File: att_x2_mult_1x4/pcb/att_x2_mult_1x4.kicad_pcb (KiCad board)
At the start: 2 copper layers, 17.8 x 95.2 mm, 13 parts, among them J1 AudioJack2_SwitchT, J2 AudioJack2_SwitchT, J3 AudioJack2_SwitchT, J4 AudioJack2_SwitchT, J5 AudioJack2_SwitchT, J6 AudioJack2_SwitchT, J7 AudioJack2_SwitchT, J8 AudioJack2_SwitchT

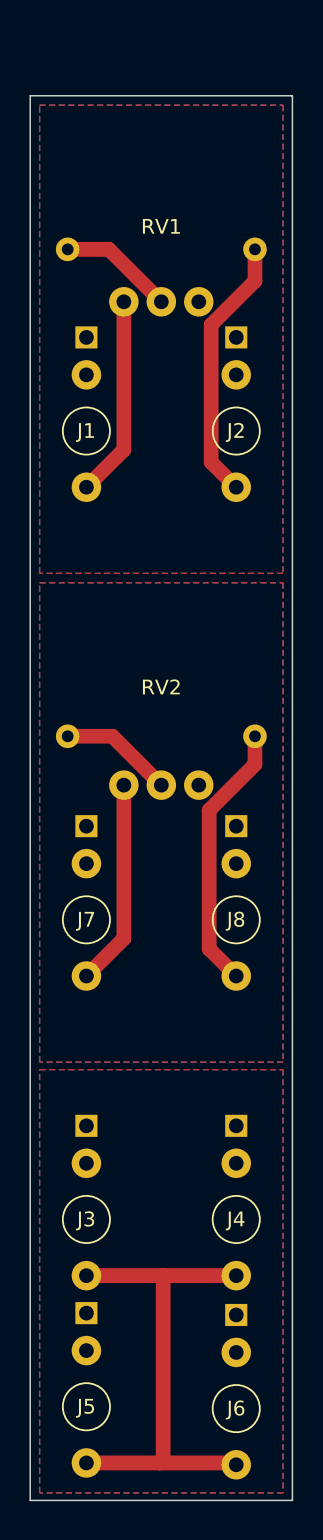
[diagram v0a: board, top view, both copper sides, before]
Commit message: moved resistor, added scale to panel
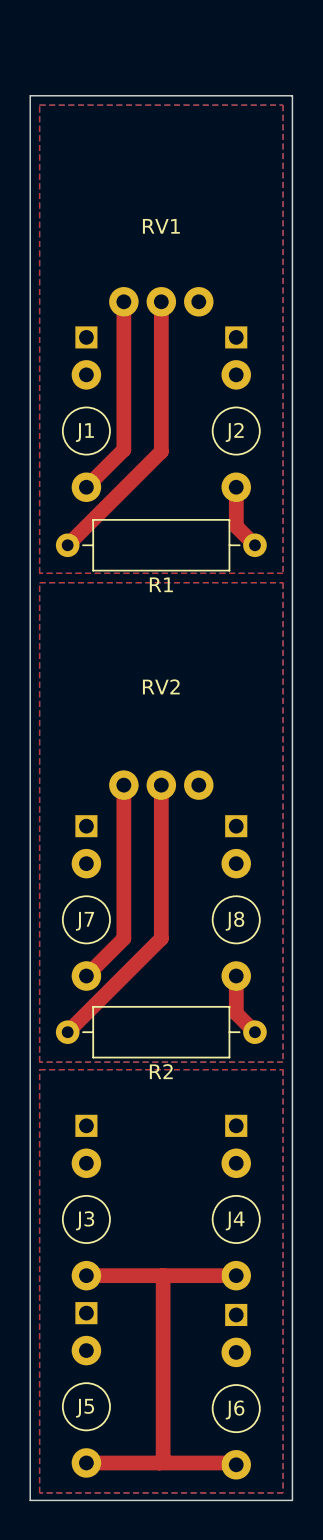
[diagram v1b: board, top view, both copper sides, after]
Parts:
- R1, R2: moved to F.Cu
- moved R1 20.1 mm to (108.0, 105.4)
- moved R2 20.1 mm to (108.0, 138.4)
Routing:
- net Net-(J8-PadT): track 18.3 -> 4.34 mm
- net Net-(J2-PadT): track 18.1 -> 4.46 mm
- net Net-(RV2-Pad2): track 7.72 -> 19.4 mm
- net Net-(RV1-Pad2): track 7.82 -> 19.1 mm
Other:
- board text added: "MB20220612"
- board text removed: "MB20220604"

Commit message: moved second attenuator slightly down
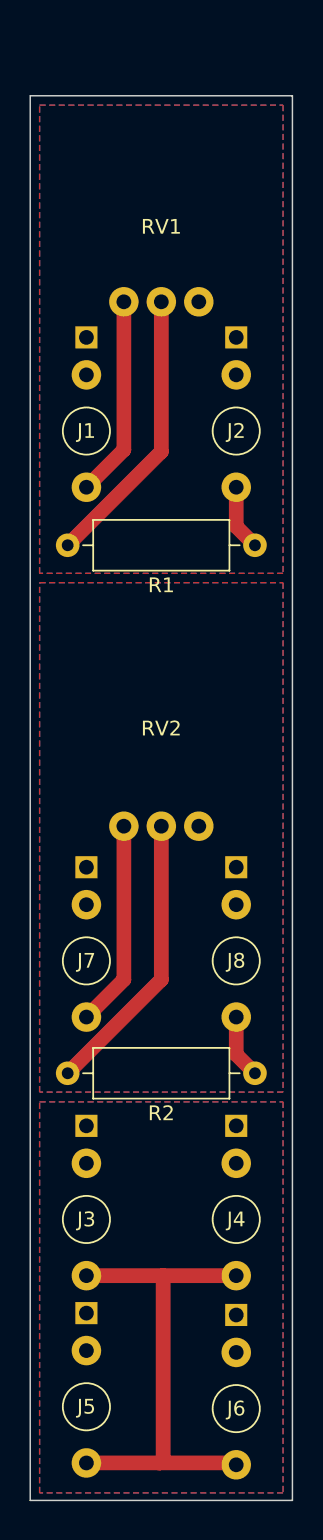
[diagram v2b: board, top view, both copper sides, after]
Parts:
- moved J7 2.78 mm to (96.5, 137.4)
- moved J8 2.78 mm to (106.7, 137.4)
- moved R2 2.78 mm to (108.0, 141.2)
- moved RV2 2.78 mm to (99.1, 124.5)
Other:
- board text added: "MB20220617"
- board text removed: "MB20220612"
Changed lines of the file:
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@@
   (net 15 "Net-(J8-PadT)")
   (net 16 "unconnected-(J8-PadTN)")
-  (net 17 "Net-(RV1-Pad2)")
-  (net 18 "Net-(RV2-Pad2)")
+  (net 17 "Net-(R1-Pad2)")
+  (net 18 "Net-(R2-Pad2)")
   (footprint "eurorack_footprints:audio_jack_pj-398sm" (layer "F.Cu")
     (at 106.68 167.765)
@@
   )
   (footprint "eurorack_footprints:audio_jack_pj-398sm" (layer "F.Cu")
-    (at 96.52 134.62)
+    (at 96.52 137.404)
     (property "Sheetfile" "att_x2_mult_1x4.kicad_sch")
     (property "Sheetname" "")
@@
       (net 2 "Net-(J1-PadT)") (pinfunction "1") (pintype "passive"))
     (pad "2" thru_hole circle (at 2.54 0) (size 2 2) (drill 1) (layers *.Cu *.Mask)
-      (net 17 "Net-(RV1-Pad2)") (pinfunction "2") (pintype "passive"))
+      (net 17 "Net-(R1-Pad2)") (pinfunction "2") (pintype "passive"))
     (pad "3" thru_hole circle (at 5.08 0) (size 2 2) (drill 1) (layers *.Cu *.Mask)
       (net 1 "/gnd1") (pinfunction "3") (pintype "passive"))
   )
   (footprint "Resistor_THT:R_Axial_DIN0309_L9.0mm_D3.2mm_P12.70mm_Horizontal" (layer "F.Cu")
-    (at 107.95 138.43 180)
+    (at 107.95 141.214 180)
     (descr "Resistor, Axial_DIN0309 series, Axial, Horizontal, pin pitch=12.7mm, 0.5W = 1/2W, length*diameter=9*3.2mm^2, http://cdn-reichelt.de/documents/datenblatt/B400/1_4W%23YAG.pdf")
     (tags "Resistor Axial_DIN0309 series Axial Horizontal pin pitch 12.7mm 0.5W = 1/2W length 9mm diameter 3.2mm")
@@
       (net 15 "Net-(J8-PadT)") (pintype "passive"))
     (pad "2" thru_hole oval (at 12.7 0 180) (size 1.6 1.6) (drill 0.8) (layers *.Cu *.Mask)
-      (net 18 "Net-(RV2-Pad2)") (pintype "passive"))
+      (net 18 "Net-(R2-Pad2)") (pintype "passive"))
     (model "${KICAD6_3DMODEL_DIR}/Resistor_THT.3dshapes/R_Axial_DIN0309_L9.0mm_D3.2mm_P12.70mm_Horizontal.wrl"
       (offset (xyz 0 0 0))
@@
   )
   (footprint "eurorack_footprints:pot1_A" (layer "F.Cu")
-    (at 99.06 121.6765)
+    (at 99.06 124.4605)
     (property "Sheetfile" "att_x2_mult_1x4.kicad_sch")
     (property "Sheetname" "")
@@
       (net 13 "Net-(J7-PadT)") (pinfunction "1") (pintype "passive"))
     (pad "2" thru_hole circle (at 2.54 0) (size 2 2) (drill 1) (layers *.Cu *.Mask)
-      (net 18 "Net-(RV2-Pad2)") (pinfunction "2") (pintype "passive"))
+      (net 18 "Net-(R2-Pad2)") (pinfunction "2") (pintype "passive"))
     (pad "3" thru_hole circle (at 5.08 0) (size 2 2) (drill 1) (layers *.Cu *.Mask)
       (net 12 "/gnd2") (pinfunction "3") (pintype "passive"))
@@
   )
   (footprint "eurorack_footprints:audio_jack_pj-398sm" (layer "F.Cu")
-    (at 106.68 134.62)
+    (at 106.68 137.404)
     (property "Sheetfile" "att_x2_mult_1x4.kicad_sch")
     (property "Sheetname" "")
@@
       (net 4 "Net-(J2-PadT)") (pintype "passive"))
     (pad "2" thru_hole oval (at 12.7 0 180) (size 1.6 1.6) (drill 0.8) (layers *.Cu *.Mask)
-      (net 17 "Net-(RV1-Pad2)") (pintype "passive"))
+      (net 17 "Net-(R1-Pad2)") (pintype "passive"))
     (model "${KICAD6_3DMODEL_DIR}/Resistor_THT.3dshapes/R_Axial_DIN0309_L9.0mm_D3.2mm_P12.70mm_Horizontal.wrl"
       (offset (xyz 0 0 0))
@@
     (effects (font (size 1.5 1.5) (thickness 0.3)) (justify mirror))
   )
-  (gr_text "MB20220612\n" (at 101.6 165.1) (layer "B.SilkS")
+  (gr_text "MB20220617\n" (at 101.6 165.1) (layer "B.SilkS")
     (effects (font (size 1 1) (thickness 0.15)) (justify mirror))
   )
@@
   (segment (start 101.475 167.64) (end 106.555 167.64) (width 1) (layer "F.Cu") (net 7))
   (segment (start 101.725 154.94) (end 101.725 167.39) (width 1) (layer "F.Cu") (net 7))
-  (segment (start 99.06 132.08) (end 99.06 122.045) (width 1) (layer "F.Cu") (net 13))
-  (segment (start 96.52 134.62) (end 99.06 132.08) (width 1) (layer "F.Cu") (net 13))
-  (segment (start 106.68 134.62) (end 106.68 137.16) (width 1) (layer "F.Cu") (net 15))
-  (segment (start 106.68 137.16) (end 107.95 138.43) (width 1) (layer "F.Cu") (net 15))
+  (segment (start 99.06 134.864) (end 99.06 124.829) (width 1) (layer "F.Cu") (net 13))
+  (segment (start 96.52 137.404) (end 99.06 134.864) (width 1) (layer "F.Cu") (net 13))
+  (segment (start 106.68 137.404) (end 106.68 139.944) (width 1) (layer "F.Cu") (net 15))
+  (segment (start 106.68 139.944) (end 107.95 141.214) (width 1) (layer "F.Cu") (net 15))
   (segment (start 95.25 105.41) (end 101.6 99.06) (width 1) (layer "F.Cu") (net 17))
   (segment (start 101.6 99.06) (end 101.6 88.9) (width 1) (layer "F.Cu") (net 17))
-  (segment (start 95.25 138.43) (end 101.6 132.08) (width 1) (layer "F.Cu") (net 18))
-  (segment (start 101.6 132.08) (end 101.6 121.6765) (width 1) (layer "F.Cu") (net 18))
+  (segment (start 95.25 141.214) (end 101.6 134.864) (width 1) (layer "F.Cu") (net 18))
+  (segment (start 101.6 134.864) (end 101.6 124.4605) (width 1) (layer "F.Cu") (net 18))
   (zone (net 6) (net_name "/gnd3") (layers F&B.Cu) (hatch edge 0.508)
     (connect_pads (clearance 0.508))
@@
         (xy 109.855 169.67)
         (xy 93.345 169.67)
-        (xy 93.345 140.97)
-        (xy 109.855 140.97)
+        (xy 93.345 143.1544)
+        (xy 109.855 143.1544)
       )
     )
@@
     (polygon
       (pts
-        (xy 109.855 140.46)
-        (xy 93.345 140.46)
+        (xy 109.855 142.492)
+        (xy 93.345 142.492)
         (xy 93.345 107.95)
         (xy 109.855 107.95)

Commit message: replaced tht resistor with an smd
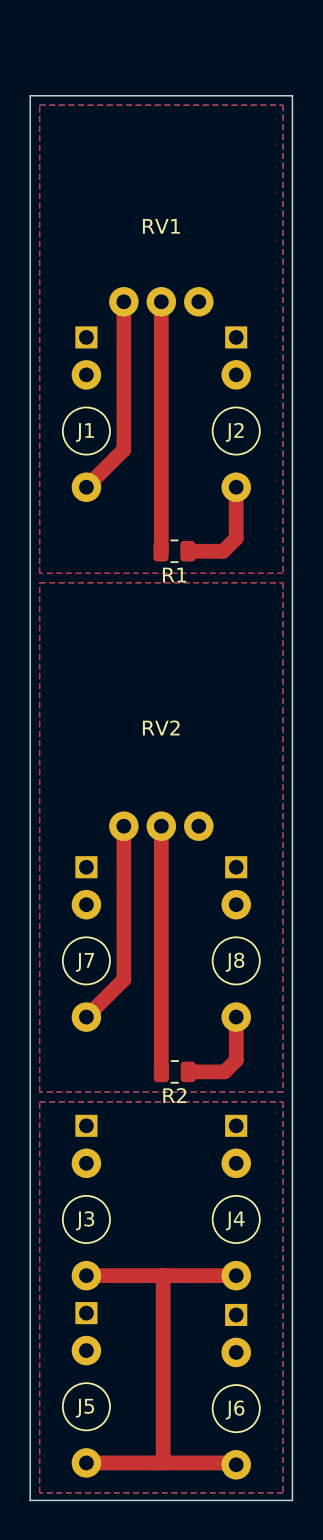
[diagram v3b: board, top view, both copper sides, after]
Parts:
- R1, R2: footprint Resistor_THT:R_Axial_DIN0309_L9.0mm_D3.2mm_P12.70mm_Horizontal -> Resistor_SMD:R_0805_2012Metric
- moved R1 5.48 mm to (102.5, 105.8)
- moved R2 5.44 mm to (102.5, 141.1)
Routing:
- net Net-(R2-Pad2): track 19.4 -> 16.2 mm
- net Net-(J2-PadT): track 4.46 -> 7.11 mm
- net Net-(R1-Pad2): track 19.1 -> 16.9 mm
- net Net-(J8-PadT): track 4.34 -> 6.51 mm

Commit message: updated pot footprint, changed rout back to tht
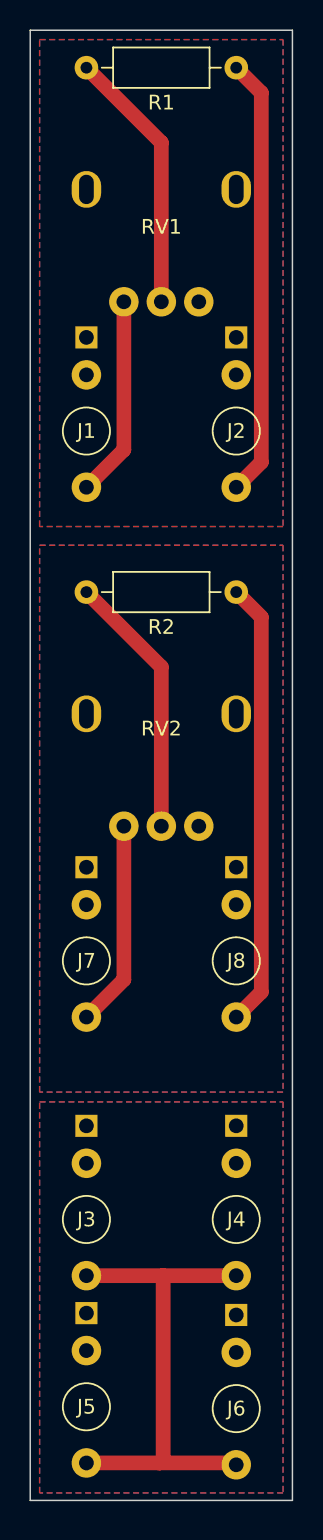
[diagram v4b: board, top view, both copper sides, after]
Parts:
- R1, R2: footprint Resistor_SMD:R_0805_2012Metric -> Resistor_THT:R_Axial_DIN0207_L6.3mm_D2.5mm_P10.16mm_Horizontal
- moved R1 33.1 mm to (106.7, 73.0)
- moved R2 32.8 mm to (106.7, 108.6)
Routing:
- net Net-(J8-PadT): track 6.51 -> 30.2 mm
- net Net-(J2-PadT): track 7.11 -> 29.9 mm
- net Net-(R2-Pad2): track 16.2 -> 18.0 mm
- net Net-(R1-Pad2): track 16.9 -> 18.0 mm
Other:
- board size 17.8 x 95.2 mm -> 17.8 x 99.7 mm
- board text added: "MB20220622"
- board text removed: "MB20220617"

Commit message: reverted panel ; change pot direction
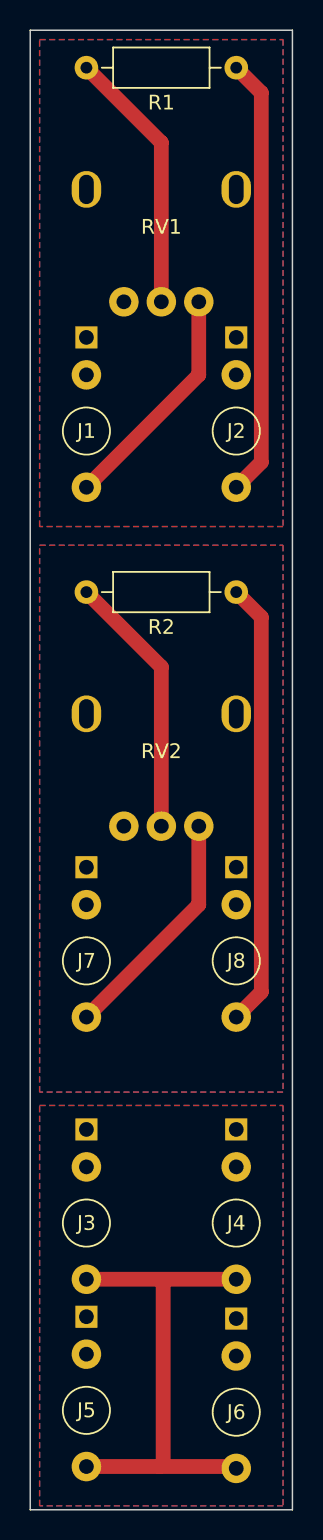
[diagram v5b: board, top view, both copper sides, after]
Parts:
- RV1, RV2: footprint eurorack_footprints:pot1_A -> eurorack_footprints:pot1_B
- moved G*** 0.24 mm to (101.6, 151.4)
- moved J3 0.24 mm to (96.5, 155.2)
- moved J4 0.24 mm to (106.7, 155.2)
- moved J5 0.24 mm to (96.5, 167.9)
- moved J6 0.24 mm to (106.7, 168.0)
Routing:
- net Net-(J7-PadT): track 13.6 -> 16.1 mm
- net Net-(J1-PadT): track 13.6 -> 15.7 mm
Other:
- board size 17.8 x 99.7 mm -> 17.8 x 100.3 mm
- board text added: "MB20220708"
- board text removed: "MB20220622"
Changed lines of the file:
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@@
   (net 18 "Net-(R2-Pad2)")
   (footprint "eurorack_footprints:audio_jack_pj-398sm" (layer "F.Cu")
-    (at 106.68 167.765)
+    (at 106.68 168.00884)
     (property "Sheetfile" "att_x2_mult_1x4.kicad_sch")
     (property "Sheetname" "")
@@
   )
   (footprint "eurorack_footprints:audio_jack_pj-398sm" (layer "F.Cu")
-    (at 96.52 154.94)
+    (at 96.52 155.18384)
     (property "Sheetfile" "att_x2_mult_1x4.kicad_sch")
     (property "Sheetname" "")
@@
       (net 8 "unconnected-(J3-PadTN)") (pintype "passive"))
   )
-  (footprint "eurorack_footprints:pot1_A" (layer "F.Cu")
+  (footprint "eurorack_footprints:pot1_B" (layer "F.Cu")
     (at 99.06 88.9)
     (property "Sheetfile" "att_x2_mult_1x4.kicad_sch")
@@
     (pad "" thru_hole oval (at 7.62 -7.62 90) (size 2.5 2) (drill oval 2 1) (layers *.Cu *.Mask))
     (pad "" thru_hole oval (at -2.54 -7.62 90) (size 2.5 2) (drill oval 2 1) (layers *.Cu *.Mask))
-    (pad "1" thru_hole circle (at 0 0) (size 2 2) (drill 1) (layers *.Cu *.Mask)
+    (pad "1" thru_hole circle (at 5.08 0) (size 2 2) (drill 1) (layers *.Cu *.Mask)
       (net 2 "Net-(J1-PadT)") (pinfunction "1") (pintype "passive"))
     (pad "2" thru_hole circle (at 2.54 0) (size 2 2) (drill 1) (layers *.Cu *.Mask)
       (net 17 "Net-(R1-Pad2)") (pinfunction "2") (pintype "passive"))
-    (pad "3" thru_hole circle (at 5.08 0) (size 2 2) (drill 1) (layers *.Cu *.Mask)
+    (pad "3" thru_hole circle (at 0 0) (size 2 2) (drill 1) (layers *.Cu *.Mask)
       (net 1 "/gnd1") (pinfunction "3") (pintype "passive"))
   )
-  (footprint "eurorack_footprints:pot1_A" (layer "F.Cu")
+  (footprint "eurorack_footprints:pot1_B" (layer "F.Cu")
     (at 99.06 124.4605)
     (property "Sheetfile" "att_x2_mult_1x4.kicad_sch")
     (property "Sheetname" "")
     (attr through_hole)
-    (fp_text reference "RV2" (at 2.54 -6.6165 unlocked) (layer "F.SilkS")
+    (fp_text reference "RV2" (at 2.54 -5.08 unlocked) (layer "F.SilkS")
       (effects (font (size 1 1) (thickness 0.15)))
     )
@@
     )
     (fp_rect (start -2.54 0) (end 7.62 -12.7) (layer "F.CrtYd") (width 0.05) (fill none))
+    (pad "" thru_hole oval (at 7.62 -7.62 90) (size 2.5 2) (drill oval 2 1) (layers *.Cu *.Mask))
     (pad "" thru_hole oval (at -2.54 -7.62 90) (size 2.5 2) (drill oval 2 1) (layers *.Cu *.Mask))
-    (pad "" thru_hole oval (at 7.62 -7.62 90) (size 2.5 2) (drill oval 2 1) (layers *.Cu *.Mask))
-    (pad "1" thru_hole circle (at 0 0) (size 2 2) (drill 1) (layers *.Cu *.Mask)
+    (pad "1" thru_hole circle (at 5.08 0) (size 2 2) (drill 1) (layers *.Cu *.Mask)
       (net 13 "Net-(J7-PadT)") (pinfunction "1") (pintype "passive"))
     (pad "2" thru_hole circle (at 2.54 0) (size 2 2) (drill 1) (layers *.Cu *.Mask)
       (net 18 "Net-(R2-Pad2)") (pinfunction "2") (pintype "passive"))
-    (pad "3" thru_hole circle (at 5.08 0) (size 2 2) (drill 1) (layers *.Cu *.Mask)
+    (pad "3" thru_hole circle (at 0 0) (size 2 2) (drill 1) (layers *.Cu *.Mask)
       (net 12 "/gnd2") (pinfunction "3") (pintype "passive"))
   )
@@
   )
   (footprint "eurorack_footprints:audio_jack_pj-398sm" (layer "F.Cu")
-    (at 96.52 167.64)
+    (at 96.52 167.88384)
     (property "Sheetfile" "att_x2_mult_1x4.kicad_sch")
     (property "Sheetname" "")
@@
   )
   (footprint "eurorack_footprints:audio_jack_pj-398sm" (layer "F.Cu")
-    (at 106.68 154.94)
+    (at 106.68 155.18384)
     (property "Sheetfile" "att_x2_mult_1x4.kicad_sch")
     (property "Sheetname" "")
@@
   )
   (footprint "eurorack_footprints:musikbeton_8mm_front" (layer "B.Cu")
-    (at 101.6 151.13 180)
+    (at 101.6 151.37384 180)
     (attr board_only exclude_from_pos_files exclude_from_bom)
     (fp_text reference "G***" (at 0 0) (layer "B.SilkS") hide
@@
     )
   )
-  (gr_rect (start 92.71 70.485) (end 110.49 170.18) (layer "Edge.Cuts") (width 0.1) (fill none))
+  (gr_rect (start 92.71 70.485) (end 110.49 170.815) (layer "Edge.Cuts") (width 0.1) (fill none))
   (gr_text "RoHS" (at 106.045 77.47) (layer "B.SilkS")
     (effects (font (size 1.5 1.5) (thickness 0.3)) (justify mirror))
   )
-  (gr_text "MB20220622\n" (at 101.6 165.1) (layer "B.SilkS")
+  (gr_text "MB20220708\n" (at 101.6 165.34384) (layer "B.SilkS")
     (effects (font (size 1 1) (thickness 0.15)) (justify mirror))
   )
-  (segment (start 96.52 101.475) (end 99.06 98.935) (width 1) (layer "F.Cu") (net 2))
-  (segment (start 99.06 98.935) (end 99.06 88.9) (width 1) (layer "F.Cu") (net 2))
+  (segment (start 96.52 101.475) (end 104.14 93.855) (width 1) (layer "F.Cu") (net 2))
+  (segment (start 104.14 93.855) (end 104.14 88.9) (width 1) (layer "F.Cu") (net 2))
   (segment (start 108.379511 74.724511) (end 108.379511 99.775489) (width 1) (layer "F.Cu") (net 4))
   (segment (start 108.379511 99.775489) (end 106.68 101.475) (width 1) (layer "F.Cu") (net 4))
-  (segment (start 106.68 101.475) (end 106.677525 101.477475) (width 1) (layer "F.Cu") (net 4))
   (segment (start 106.68 73.025) (end 108.379511 74.724511) (width 1) (layer "F.Cu") (net 4))
-  (segment (start 101.725 154.94) (end 106.68 154.94) (width 1) (layer "F.Cu") (net 7))
-  (segment (start 101.725 167.39) (end 101.475 167.64) (width 1) (layer "F.Cu") (net 7))
-  (segment (start 96.52 154.94) (end 101.725 154.94) (width 1) (layer "F.Cu") (net 7))
-  (segment (start 106.555 167.64) (end 106.68 167.765) (width 1) (layer "F.Cu") (net 7))
-  (segment (start 96.52 167.64) (end 101.475 167.64) (width 1) (layer "F.Cu") (net 7))
-  (segment (start 101.475 167.64) (end 106.555 167.64) (width 1) (layer "F.Cu") (net 7))
-  (segment (start 101.725 154.94) (end 101.725 167.39) (width 1) (layer "F.Cu") (net 7))
-  (segment (start 99.06 134.864) (end 99.06 124.829) (width 1) (layer "F.Cu") (net 13))
-  (segment (start 96.52 137.404) (end 99.06 134.864) (width 1) (layer "F.Cu") (net 13))
+  (segment (start 101.725 155.18384) (end 106.68 155.18384) (width 1) (layer "F.Cu") (net 7))
+  (segment (start 101.725 167.63384) (end 101.475 167.88384) (width 1) (layer "F.Cu") (net 7))
+  (segment (start 96.52 155.18384) (end 101.725 155.18384) (width 1) (layer "F.Cu") (net 7))
+  (segment (start 106.555 167.88384) (end 106.68 168.00884) (width 1) (layer "F.Cu") (net 7))
+  (segment (start 96.52 167.88384) (end 101.475 167.88384) (width 1) (layer "F.Cu") (net 7))
+  (segment (start 101.475 167.88384) (end 106.555 167.88384) (width 1) (layer "F.Cu") (net 7))
+  (segment (start 101.725 155.18384) (end 101.725 167.63384) (width 1) (layer "F.Cu") (net 7))
+  (segment (start 96.52 137.404) (end 104.14 129.784) (width 1) (layer "F.Cu") (net 13))
+  (segment (start 104.14 129.784) (end 104.14 124.4605) (width 1) (layer "F.Cu") (net 13))
   (segment (start 106.68 137.404) (end 108.37952 135.70448) (width 1) (layer "F.Cu") (net 15))
   (segment (start 108.37952 110.28452) (end 106.68 108.585) (width 1) (layer "F.Cu") (net 15))
@@
     (polygon
       (pts
-        (xy 109.855 169.67)
-        (xy 93.345 169.67)
-        (xy 93.345 143.1544)
-        (xy 109.855 143.1544)
+        (xy 109.855 170.54884)
+        (xy 93.345 170.54884)
+        (xy 93.345 143.39824)
+        (xy 109.855 143.39824)
       )
     )
